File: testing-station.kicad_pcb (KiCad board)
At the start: 4 copper layers, 82.3 x 53.9 mm, 83 parts, among them IC1 BME680, IC2 DS3231, IC3 74HC4050D, J1 pyranometer, J10 Conn_01x06_Socket, J11 Conn_01x08_Socket, J13 microSD, J2 anemometer, J3 AM2315C, J4 FPC connector, J5 Pt100, J6 Conn_01x10_Socket, J7 Pt100, J8 Conn_01x08_Socket, J9 Pt100, Q1 BSS138, SW1 500SSP1S2M2QEA, U1 TBA_1-0519, U2 MAX31865, U4 MAX31865, U6 MAX31865

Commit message: BOM update
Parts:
- renumbered SJ1 to JP10

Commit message: small layout change PCB
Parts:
- moved D2 23.1 mm to (133.8, 114.3), turned to 90 degrees
- moved D1 20.7 mm to (133.8, 109.0), turned to 90 degrees
- moved J1 16.1 mm to (144.2, 90.8)
- moved SW1 12.0 mm to (139.4, 111.9), turned to 90 degrees
- moved J13 7.76 mm to (123.9, 111.8)
- moved R3 7.29 mm to (133.6, 98.8), turned to -90 degrees
- moved R2 5.71 mm to (133.6, 93.7), turned to -90 degrees
- moved J4 4.08 mm to (152.1, 111.3)
- moved R25 0.06 mm to (190.3, 119.2)
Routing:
- net /MISO: track 119.2 -> 158.8 mm, vias 3 -> 10
- net /D8: track 32.1 -> 60.1 mm, vias 2 -> 1
- net /D2: track 18.7 -> 45.7 mm
- net +9V: track 83.8 -> 108.8 mm, vias 1 -> 2
- net Net-(D2-K): track 2.26 -> 23.8 mm
- net Net-(D1-K): track 2.26 -> 21.9 mm
- net Net-(J9-Pin_4): track 60.7 -> 42.2 mm, vias 1 -> 2
- net /A5: track 23.6 -> 40.9 mm
- net /D9: track 57.1 -> 71.0 mm, vias 0 -> 3
- net /microSD/3Y: track 71.1 -> 83.4 mm, vias 0 -> 2
- net GND: track 50.5 -> 62.6 mm, vias 14 -> 20
- net +5V: track 116.6 -> 127.2 mm, vias 1 -> 2
- net /microSD/1Y: track 62.0 -> 71.1 mm
- net /SCK: track 102.9 -> 111.7 mm
- net /microSD/2Y: track 57.9 -> 66.4 mm
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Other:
- board size 82.3 x 53.9 mm -> 83.2 x 53.9 mm

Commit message: silkscreen update
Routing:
- net /D7: track 43.0 -> 41.6 mm
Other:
- board text added: "<Temp out"
- board text added: "OFF"
- board text added: "ON"
- board text added: "Pot1"
- board text added: "Pot2"
- board text added: "Pot3"
- board text added: "Solar irr>"
- board text added: "Wind"
- board text added: "black"
- board text added: "red"
- board text added: "white"
- board text added: "yellow"
- board text removed: "fffff"

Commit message: implemented Eurocircuits design remarks
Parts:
- FB1, FB2, FB3: footprint Inductor_SMD:L_0805_2012Metric -> external_footprints:LI0805G201R-10
- U2, U4, U6: footprint Package_DFN_QFN:TQFN-20-1EP_5x5mm_P0.65mm_EP3.25x3.25mm -> external_footprints:MAX31865ATP+
- moved FB3 0.14 mm to (173.6, 87.1)
- moved FB1 0.14 mm to (163.2, 111.1)
- moved FB2 0.11 mm to (160.0, 87.7)
- turned J4 to 180 degrees
- turned U2 to 0 degrees
- turned U4 to 180 degrees
- turned U6 to 180 degrees
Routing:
- net GND: track 62.2 -> 44.3 mm
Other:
- board text added: "<temp out"
- board text added: "pot1"
- board text added: "pot2"
- board text added: "pot3"
- board text added: "solar irr>"
- board text added: "wind"
- board text removed: "<Temp out"
- board text removed: "Pot1"
- board text removed: "Pot2"
- board text removed: "Pot3"
- board text removed: "Solar irr>"
- board text removed: "Wind"

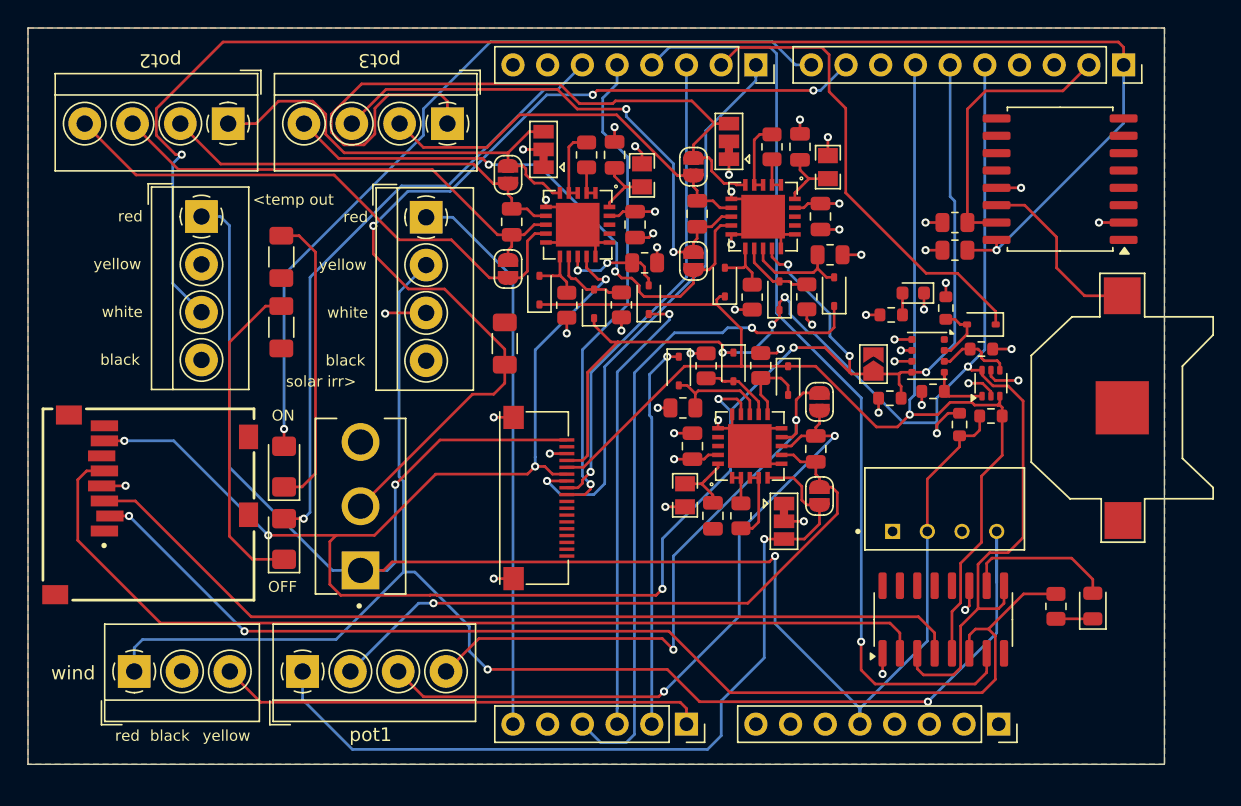
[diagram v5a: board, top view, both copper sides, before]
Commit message: final on/off LED update
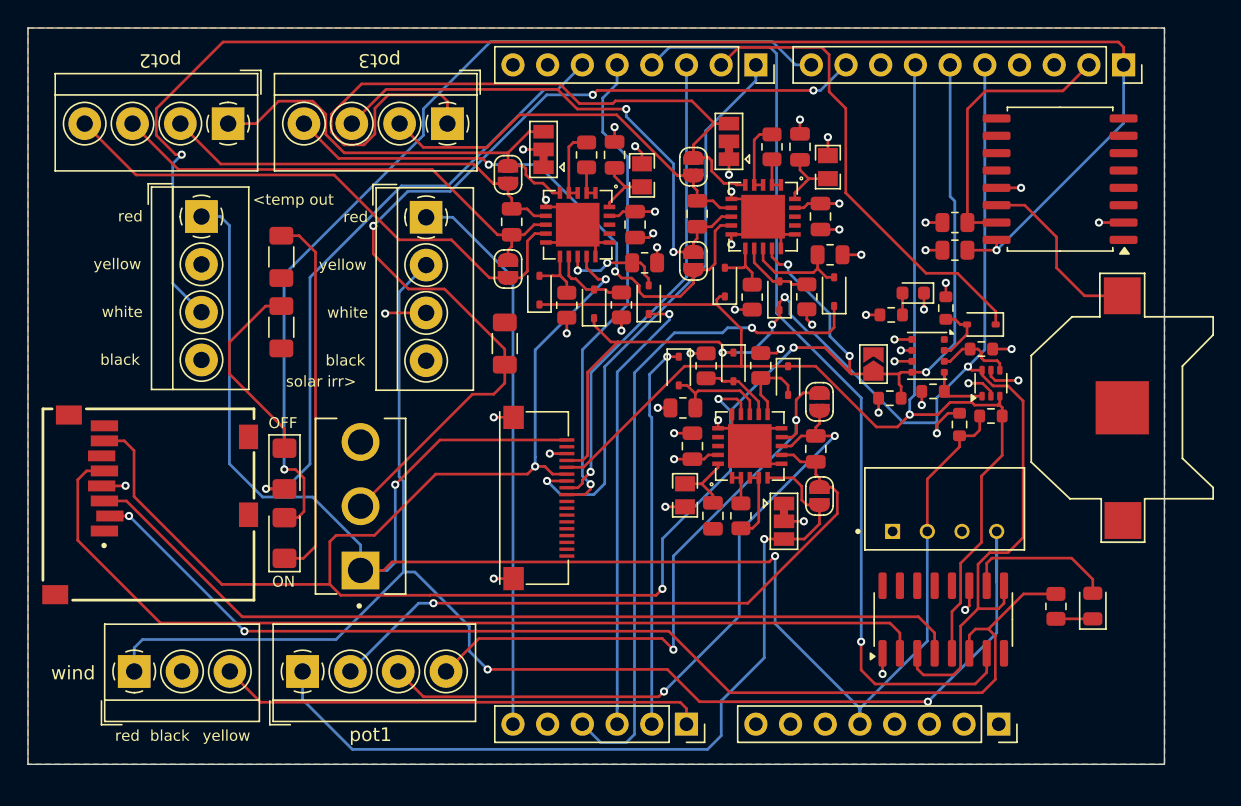
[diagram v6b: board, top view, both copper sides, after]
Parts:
- moved D1 5.23 mm to (133.8, 114.2)
- moved D2 5.16 mm to (133.8, 109.1), turned to -90 degrees
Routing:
- net Net-(D2-K): track 23.8 -> 14.3 mm
- net /D8: track 60.1 -> 67.5 mm
- net Net-(D1-K): track 21.9 -> 27.2 mm
- net /MISO: track 159.4 -> 162.4 mm, vias 10 -> 8
- net +5V: track 127.2 -> 128.1 mm

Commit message: BOM presets update
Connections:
- IC2 pad 15: /SCA -> /SDA
- J6 pad 2: /SCA -> /SDA
- R24 pad 2: /SCA -> /SDA
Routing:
- net /SDA: track 0.00 -> 20.7 mm
- net /SCA: track 20.7 -> 0.00 mm

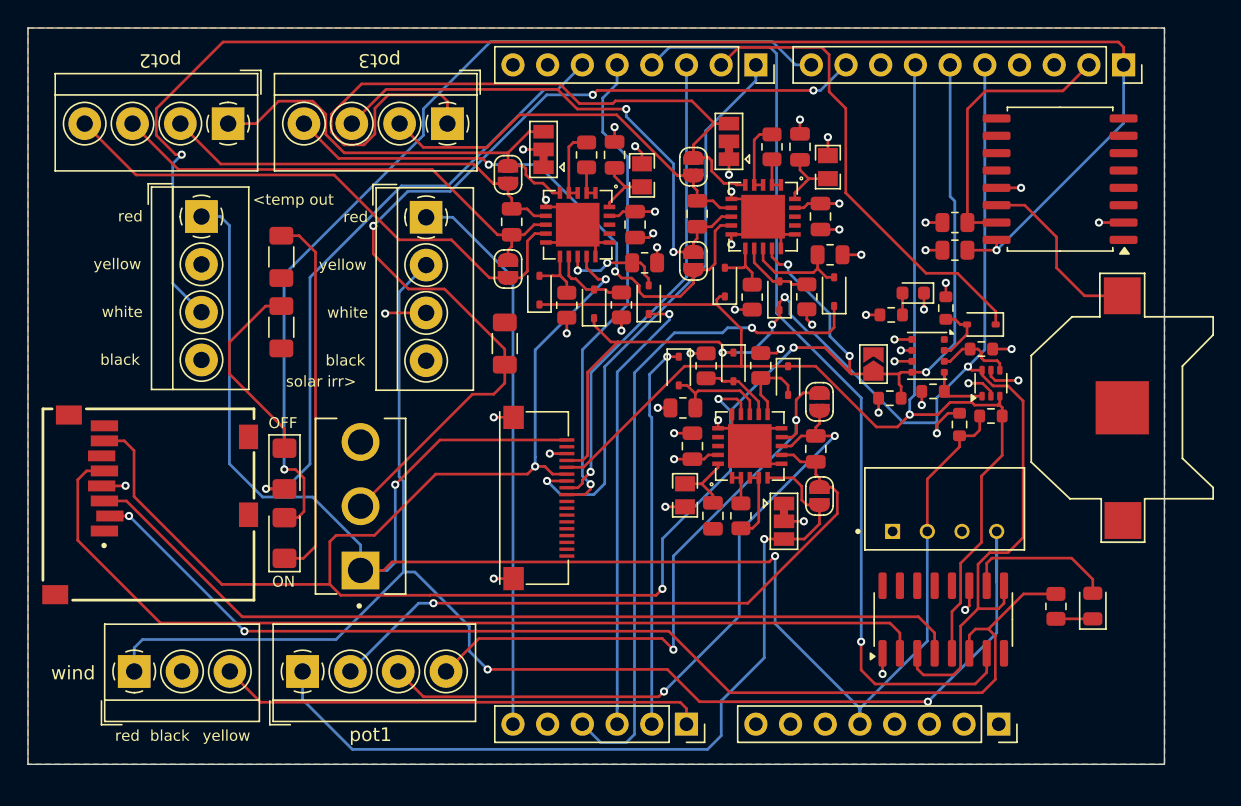
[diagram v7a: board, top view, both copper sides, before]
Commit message: compacter PCB design + debugging improvements pyranometer pin change, AM2315C I2C wiring fix, changed stackup, added ground vias, double sided PCB
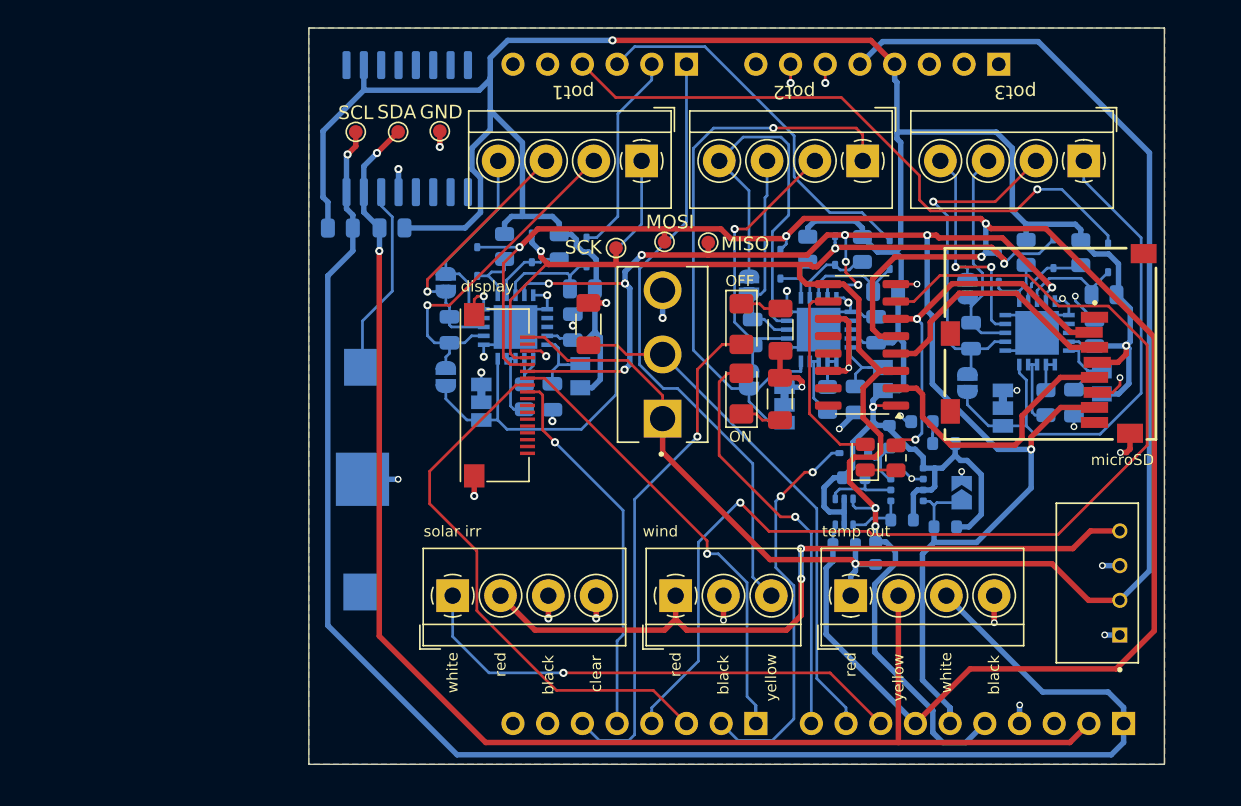
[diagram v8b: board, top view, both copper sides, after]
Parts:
- added TP1: MOSI, TestPoint:TestPoint_Pad_D1.0mm, F.Cu at (161.7, 92.5)
- added TP2: MISO, TestPoint:TestPoint_Pad_D1.0mm, F.Cu at (164.8, 92.6)
- added TP3: SCK, TestPoint:TestPoint_Pad_D1.0mm, F.Cu at (158.1, 93.0)
- added TP4: SDA, TestPoint:TestPoint_Pad_D1.0mm, F.Cu at (142.2, 84.5)
- added TP5: SCL, TestPoint:TestPoint_Pad_D1.0mm, F.Cu at (139.1, 84.5)
- added TP6: GND, TestPoint:TestPoint_Pad_D1.0mm, F.Cu at (145.2, 84.5)
- B1, C1, C11, C12, C13, C2, C3, C6, C7, C8, D10, D11, D12, D13, D3, D4, D5, D6, D7, D8, D9, FB1, FB2, FB3, IC1, IC2, J10, J11, J6, J8, JP1, JP10, JP2, JP3, JP4, JP5, JP6, JP7, JP8, JP9, Q1, R10, R11, R12, R13, R14, R15, R16, R17, R18, R19, R20, R21, R22, R23, R24, R4, R5, R6, R7, R8, R9, U2, U4, U6: moved to B.Cu
- moved J13 67.1 mm to (189.9, 100.0), turned to 90 degrees
- moved B1 55.9 mm to (139.5, 109.9)
- moved J3 55.0 mm to (175.3, 118.5), turned to 0 degrees
- moved J10 48.3 mm to (163.3, 79.5), turned to 90 degrees
- moved J11 48.3 mm to (186.1, 79.5), turned to 90 degrees
- moved J6 48.2 mm to (195.3, 127.8), turned to 90 degrees
- moved J8 48.2 mm to (168.3, 127.8), turned to 90 degrees
- moved IC2 47.9 mm to (142.8, 84.3), turned to -90 degrees
- moved J9 46.7 mm to (192.3, 86.6)
- moved J7 46.5 mm to (176.2, 86.6)
- moved R23 45.0 mm to (137.9, 91.5)
- moved J5 44.9 mm to (160.0, 86.6), turned to 180 degrees
- moved R24 41.2 mm to (141.7, 91.5), turned to 180 degrees
- moved J2 40.0 mm to (162.5, 118.5)
- moved R2 38.0 mm to (170.1, 104.0), turned to 90 degrees
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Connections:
- J1 pad 1: /A5 -> /D10
- J10 pad 6: /A5 -> unconnected-(J10-Pin_6-Pad6)
- J6 pad 8: unconnected-(J6-Pin_8-Pad8) -> /D10
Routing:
- net +3.3V: track 46.3 -> 225.8 mm, vias 29 -> 3
- net /SDA: track 20.7 -> 104.9 mm, vias 0 -> 2
- net /microSD/3Y: track 83.4 -> 27.9 mm
- net +9V: track 108.8 -> 54.7 mm
- net /microSD/1Y: track 71.1 -> 20.3 mm
- net /microSD/2Y: track 66.4 -> 18.7 mm
- net /MOSI: track 103.0 -> 145.6 mm, vias 1 -> 4
- net /A5: track 40.9 -> 0.00 mm
- net GND: track 44.3 -> 85.0 mm, vias 20 -> 37
- net /D8: track 67.5 -> 30.3 mm
- net /D10: track 0.00 -> 37.0 mm, vias 0 -> 1
- net /MISO: track 162.4 -> 125.6 mm, vias 8 -> 10
- net /D9: track 71.0 -> 38.6 mm, vias 3 -> 0
- net Net-(J5-Pin_3): track 50.4 -> 19.6 mm, vias 2 -> 1
- net Net-(J5-Pin_4): track 44.4 -> 15.1 mm, vias 2 -> 0
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- added copper zone on In2.Cu, net GND
- removed copper zone on In2.Cu, net +3.3V
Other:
- board size 83.2 x 53.9 mm -> 62.6 x 53.9 mm
- board text added: "clear"
- board text added: "display"
- board text added: "microSD"
- board text added: "solar irr"
- board text added: "temp out"
- board text removed: "<temp out"
- board text removed: "solar irr>"
